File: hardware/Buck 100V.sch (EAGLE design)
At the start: 20 parts, among them M2 SI5435BDC, Q2 FMMT723, U1 LT3756EMSE

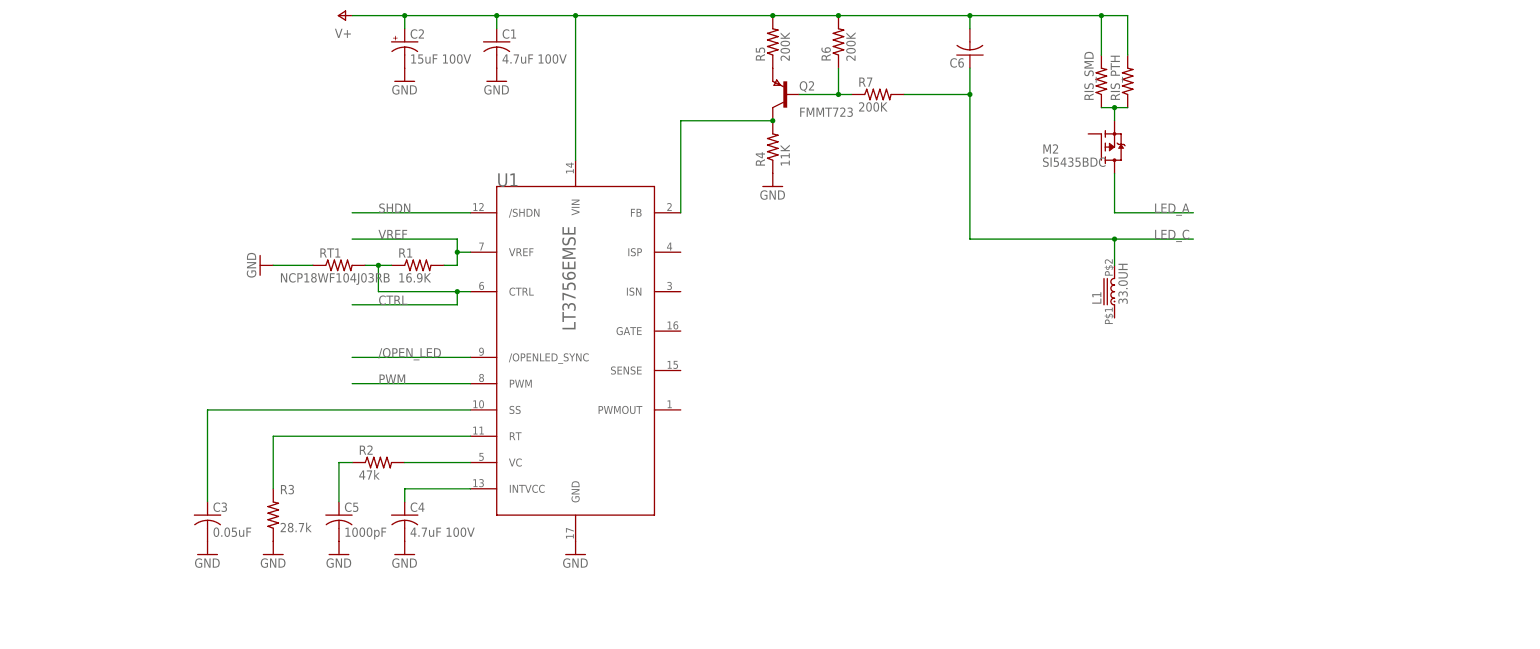
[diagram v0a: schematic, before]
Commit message: More work on Buck schematic. Now it just needs the schotkey diode, headers and double checking.
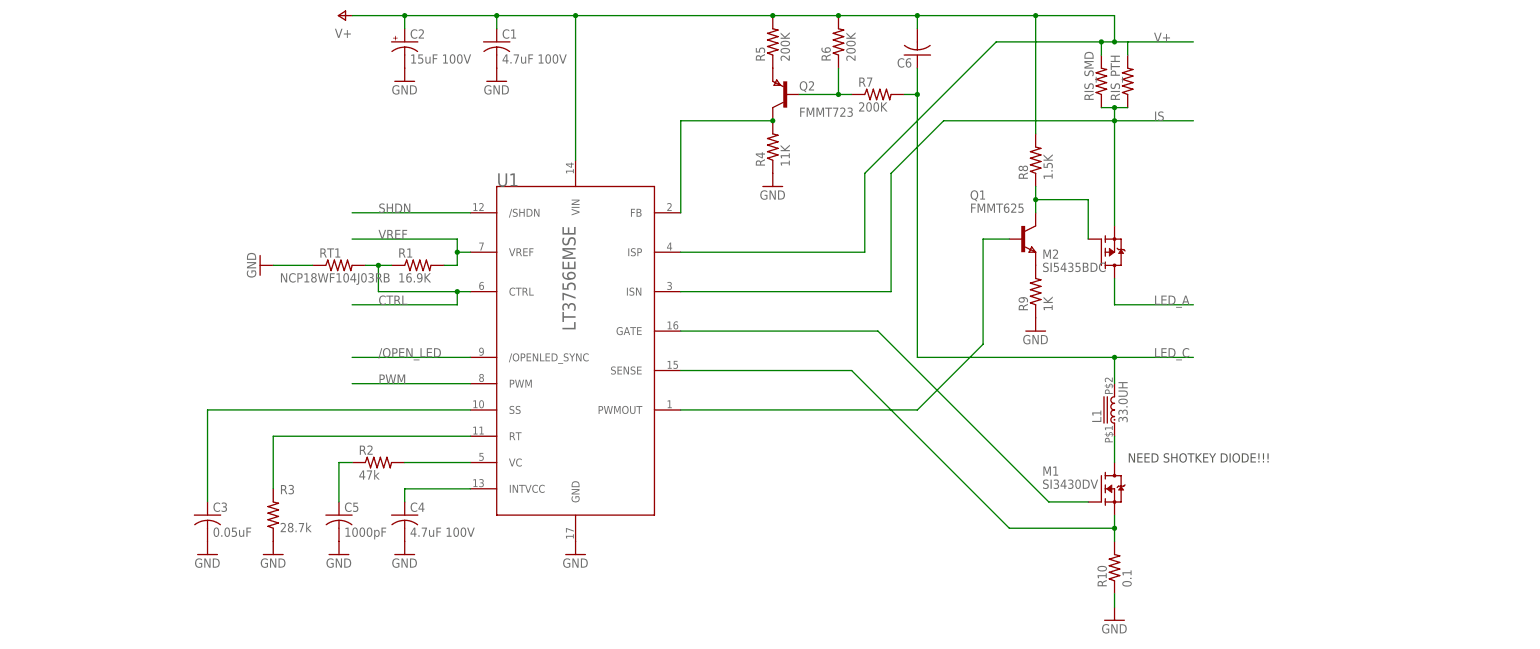
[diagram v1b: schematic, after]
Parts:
- added M1: SI3430DV, LED-drivers:SI3430DV
- added Q1: FMMT625, zetex:FMMT625
- added R10: 0.1, rcl:R-US_R0402
- added R8: 1.5K, rcl:R-US_R0402
- added R9: 1K, rcl:R-US_R0402
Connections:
- new net IS: M2.S, RIS_PTH.1, RIS_SMD.1, U1.ISN
- new net N$10: Q1.E, R9.2
- new net N$11: Q1.B, U1.PWMOUT
- new net N$12: L1.1, M1.D
- new net N$13: M1.G, U1.GATE
- new net N$14: M1.S, R10.2, U1.SENSE
- net GND: now also R10.1, R9.1
- net N$9: now also M2.G, Q1.C, R8.1; no longer M2.S, RIS_PTH.1, RIS_SMD.1
- net V+: now also R8.2, U1.ISP
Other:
- note added: "NEED SHOTKEY DIODE!!!"
- moved on the sheet: C6, L1, M2

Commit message: Add schottky diode. Change resistors and caps to 0805 for hand solderability. Still need headers and checking before starting layout. Also need reverse protection diode and possibly est protection components.
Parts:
- added D1: STPS2H100UY, diode:DIODE-SMB
- C1, C3, C4, C5: device rcl:C-USC0603 -> rcl:C-USC0805
- R1, R10, R2, R3, R4, R5, R6, R7, R8, R9, RT1: device rcl:R-US_R0402 -> rcl:R-US_R0805
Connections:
- net N$12: now also D1.A
- net V+: now also D1.C
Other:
- note removed: "NEED SHOTKEY DIODE!!!"
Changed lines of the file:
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@@
 <grid distance="0.1" unitdist="inch" unit="inch" style="lines" multiple="1" display="no" altdistance="0.01" altunitdist="inch" altunit="inch"/>
 <layers>
-<layer number="1" name="Top" color="4" fill="1" visible="no" active="no"/>
-<layer number="16" name="Bottom" color="1" fill="1" visible="no" active="no"/>
-<layer number="17" name="Pads" color="2" fill="1" visible="no" active="no"/>
-<layer number="18" name="Vias" color="2" fill="1" visible="no" active="no"/>
-<layer number="19" name="Unrouted" color="6" fill="1" visible="no" active="no"/>
-<layer number="20" name="Dimension" color="15" fill="1" visible="no" active="no"/>
-<layer number="21" name="tPlace" color="7" fill="1" visible="no" active="no"/>
-<layer number="22" name="bPlace" color="7" fill="1" visible="no" active="no"/>
-<layer number="23" name="tOrigins" color="15" fill="1" visible="no" active="no"/>
-<layer number="24" name="bOrigins" color="15" fill="1" visible="no" active="no"/>
-<layer number="25" name="tNames" color="7" fill="1" visible="no" active="no"/>
-<layer number="26" name="bNames" color="7" fill="1" visible="no" active="no"/>
-<layer number="27" name="tValues" color="7" fill="1" visible="no" active="no"/>
-<layer number="28" name="bValues" color="7" fill="1" visible="no" active="no"/>
+<layer number="1" name="Top" color="4" fill="1" visible="yes" active="no"/>
+<layer number="16" name="Bottom" color="1" fill="1" visible="yes" active="no"/>
+<layer number="17" name="Pads" color="2" fill="1" visible="yes" active="no"/>
+<layer number="18" name="Vias" color="2" fill="1" visible="yes" active="no"/>
+<layer number="19" name="Unrouted" color="6" fill="1" visible="yes" active="no"/>
+<layer number="20" name="Dimension" color="15" fill="1" visible="yes" active="no"/>
+<layer number="21" name="tPlace" color="7" fill="1" visible="yes" active="no"/>
+<layer number="22" name="bPlace" color="7" fill="1" visible="yes" active="no"/>
+<layer number="23" name="tOrigins" color="15" fill="1" visible="yes" active="no"/>
+<layer number="24" name="bOrigins" color="15" fill="1" visible="yes" active="no"/>
+<layer number="25" name="tNames" color="7" fill="1" visible="yes" active="no"/>
+<layer number="26" name="bNames" color="7" fill="1" visible="yes" active="no"/>
+<layer number="27" name="tValues" color="7" fill="1" visible="yes" active="no"/>
+<layer number="28" name="bValues" color="7" fill="1" visible="yes" active="no"/>
 <layer number="29" name="tStop" color="7" fill="3" visible="no" active="no"/>
 <layer number="30" name="bStop" color="7" fill="6" visible="no" active="no"/>
@@
 <layer number="35" name="tGlue" color="7" fill="4" visible="no" active="no"/>
 <layer number="36" name="bGlue" color="7" fill="5" visible="no" active="no"/>
-<layer number="37" name="tTest" color="7" fill="1" visible="no" active="no"/>
-<layer number="38" name="bTest" color="7" fill="1" visible="no" active="no"/>
+<layer number="37" name="tTest" color="7" fill="1" visible="yes" active="no"/>
+<layer number="38" name="bTest" color="7" fill="1" visible="yes" active="no"/>
 <layer number="39" name="tKeepout" color="4" fill="11" visible="no" active="no"/>
 <layer number="40" name="bKeepout" color="1" fill="11" visible="no" active="no"/>
@@
 <layer number="44" name="Drills" color="7" fill="1" visible="no" active="no"/>
 <layer number="45" name="Holes" color="7" fill="1" visible="no" active="no"/>
-<layer number="46" name="Milling" color="3" fill="1" visible="no" active="no"/>
-<layer number="47" name="Measures" color="7" fill="1" visible="no" active="no"/>
-<layer number="48" name="Document" color="7" fill="1" visible="no" active="no"/>
-<layer number="49" name="Reference" color="7" fill="1" visible="no" active="no"/>
-<layer number="51" name="tDocu" color="7" fill="1" visible="no" active="no"/>
-<layer number="52" name="bDocu" color="7" fill="1" visible="no" active="no"/>
+<layer number="46" name="Milling" color="3" fill="1" visible="yes" active="no"/>
+<layer number="47" name="Measures" color="7" fill="1" visible="yes" active="no"/>
+<layer number="48" name="Document" color="7" fill="1" visible="yes" active="no"/>
+<layer number="49" name="Reference" color="7" fill="1" visible="yes" active="no"/>
+<layer number="51" name="tDocu" color="7" fill="1" visible="yes" active="no"/>
+<layer number="52" name="bDocu" color="7" fill="1" visible="yes" active="no"/>
 <layer number="91" name="Nets" color="2" fill="1" visible="yes" active="yes"/>
 <layer number="92" name="Busses" color="1" fill="1" visible="yes" active="yes"/>
@@
 <part name="U1" library="LED-drivers" deviceset="LT3756" device="EMSE"/>
 <part name="GND1" library="supply1" deviceset="GND" device=""/>
-<part name="C1" library="rcl" deviceset="C-US" device="C0603" value="4.7uF 100V"/>
+<part name="C1" library="rcl" deviceset="C-US" device="C0805" value="4.7uF 100V"/>
 <part name="C2" library="rcl" deviceset="CPOL-US" device="E2,5-6E" value="15uF 100V"/>
 <part name="GND2" library="supply1" deviceset="GND" device=""/>
 <part name="GND3" library="supply1" deviceset="GND" device=""/>
 <part name="P+1" library="supply1" deviceset="V+" device=""/>
-<part name="R1" library="rcl" deviceset="R-US_" device="R0402" value="16.9K"/>
-<part name="RT1" library="rcl" deviceset="R-US_" device="R0402" value="NCP18WF104J03RB"/>
+<part name="R1" library="rcl" deviceset="R-US_" device="R0805" value="16.9K"/>
+<part name="RT1" library="rcl" deviceset="R-US_" device="R0805" value="NCP18WF104J03RB"/>
 <part name="GND4" library="supply1" deviceset="GND" device=""/>
-<part name="C3" library="rcl" deviceset="C-US" device="C0603" value="0.05uF"/>
-<part name="C4" library="rcl" deviceset="C-US" device="C0603" value="4.7uF 100V"/>
-<part name="C5" library="rcl" deviceset="C-US" device="C0603" value="1000pF"/>
-<part name="R2" library="rcl" deviceset="R-US_" device="R0402" value="47k"/>
-<part name="R3" library="rcl" deviceset="R-US_" device="R0402" value="28.7k"/>
+<part name="C3" library="rcl" deviceset="C-US" device="C0805" value="0.05uF"/>
+<part name="C4" library="rcl" deviceset="C-US" device="C0805" value="4.7uF 100V"/>
+<part name="C5" library="rcl" deviceset="C-US" device="C0805" value="1000pF"/>
+<part name="R2" library="rcl" deviceset="R-US_" device="R0805" value="47k"/>
+<part name="R3" library="rcl" deviceset="R-US_" device="R0805" value="28.7k"/>
 <part name="GND5" library="supply1" deviceset="GND" device=""/>
 <part name="GND6" library="supply1" deviceset="GND" device=""/>
@@
 <part name="RIS_PTH" library="rcl" deviceset="R-US_" device="0204/7"/>
 <part name="Q2" library="zetex" deviceset="FMMT7*" device="" technology="23"/>
-<part name="R4" library="rcl" deviceset="R-US_" device="R0402" value="11K"/>
-<part name="R5" library="rcl" deviceset="R-US_" device="R0402" value="200K"/>
-<part name="R6" library="rcl" deviceset="R-US_" device="R0402" value="200K"/>
-<part name="R7" library="rcl" deviceset="R-US_" device="R0402" value="200K"/>
+<part name="R4" library="rcl" deviceset="R-US_" device="R0805" value="11K"/>
+<part name="R5" library="rcl" deviceset="R-US_" device="R0805" value="200K"/>
+<part name="R6" library="rcl" deviceset="R-US_" device="R0805" value="200K"/>
+<part name="R7" library="rcl" deviceset="R-US_" device="R0805" value="200K"/>
 <part name="GND9" library="supply1" deviceset="GND" device=""/>
 <part name="L1" library="LED-drivers" deviceset="ASPI-0612FS" device="" value="33.0UH"/>
@@
 <part name="C6" library="rcl" deviceset="C-US" device="C2220K"/>
 <part name="Q1" library="zetex" deviceset="FMMT6*" device="" technology="25"/>
-<part name="R8" library="rcl" deviceset="R-US_" device="R0402" value="1.5K"/>
-<part name="R9" library="rcl" deviceset="R-US_" device="R0402" value="1K"/>
+<part name="R8" library="rcl" deviceset="R-US_" device="R0805" value="1.5K"/>
+<part name="R9" library="rcl" deviceset="R-US_" device="R0805" value="1K"/>
 <part name="GND10" library="supply1" deviceset="GND" device=""/>
 <part name="M1" library="LED-drivers" deviceset="SI3430DV" device=""/>
-<part name="R10" library="rcl" deviceset="R-US_" device="R0402" value="0.1"/>
+<part name="R10" library="rcl" deviceset="R-US_" device="R0805" value="0.1"/>
 <part name="GND11" library="supply1" deviceset="GND" device=""/>
+<part name="D1" library="diode" deviceset="DIODE-" device="SMB" value="STPS2H100UY"/>
+<part name="P+2" library="supply1" deviceset="V+" device=""/>
 </parts>
 <sheets>
 <sheet>
 <plain>
-<text x="106.68" y="-22.86" size="1.778" layer="97">NEED SHOTKEY DIODE!!!</text>
 </plain>
 <instances>
@@
 <instance part="R10" gate="G$1" x="104.14" y="-43.18" rot="R90"/>
 <instance part="GND11" gate="1" x="104.14" y="-53.34"/>
+<instance part="D1" gate="G$1" x="114.3" y="-20.32"/>
+<instance part="P+2" gate="1" x="124.46" y="-20.32" rot="R270"/>
 </instances>
 <busses>
@@
 <junction x="88.9" y="63.5"/>
 </segment>
+<segment>
+<pinref part="P+2" gate="1" pin="V+"/>
+<pinref part="D1" gate="G$1" pin="C"/>
+<wire x1="121.92" y1="-20.32" x2="116.84" y2="-20.32" width="0.1524" layer="91"/>
+</segment>
 </net>
 <net name="SHDN" class="0">
@@
 <pinref part="L1" gate="G$1" pin="1"/>
 <pinref part="M1" gate="G$1" pin="D"/>
-<wire x1="104.14" y1="-17.78" x2="104.14" y2="-22.86" width="0.1524" layer="91"/>
-</segment>
-</net>
+<wire x1="104.14" y1="-17.78" x2="104.14" y2="-20.32" width="0.1524" layer="91"/>
+<pinref part="D1" gate="G$1" pin="A"/>
+<wire x1="104.14" y1="-20.32" x2="104.14" y2="-22.86" width="0.1524" layer="91"/>
+<wire x1="111.76" y1="-20.32" x2="104.14" y2="-20.32" width="0.1524" layer="91"/>
+<junction x="104.14" y="-20.32"/>
+</segment>
+</net>
